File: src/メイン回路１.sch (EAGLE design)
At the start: 34 parts, among them T1 一般的なトランジスタ, T2 一般的なトランジスタ, T3 一般的なトランジスタ, T4 一般的なトランジスタ

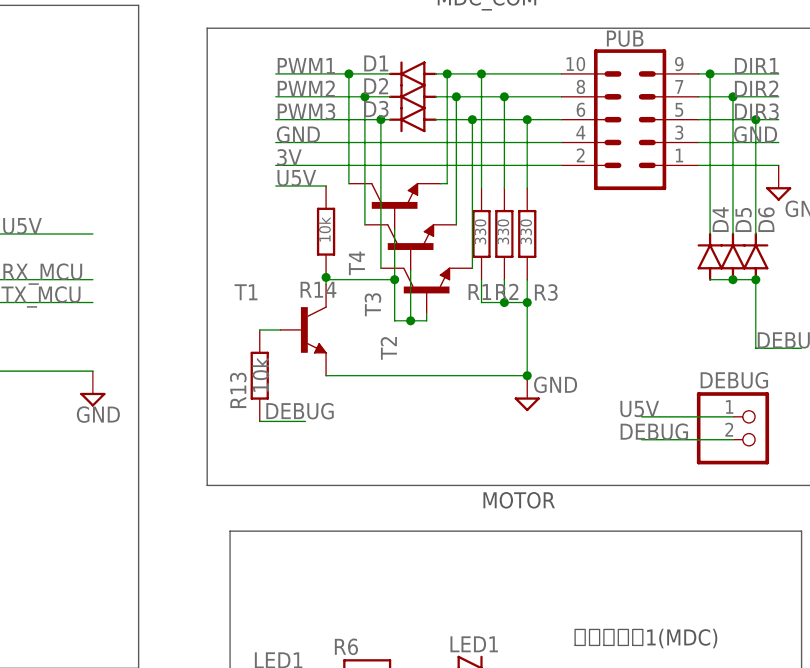
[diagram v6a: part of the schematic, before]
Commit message: 暴走対策機能付き非常停止スイッチの回路のガバを修復
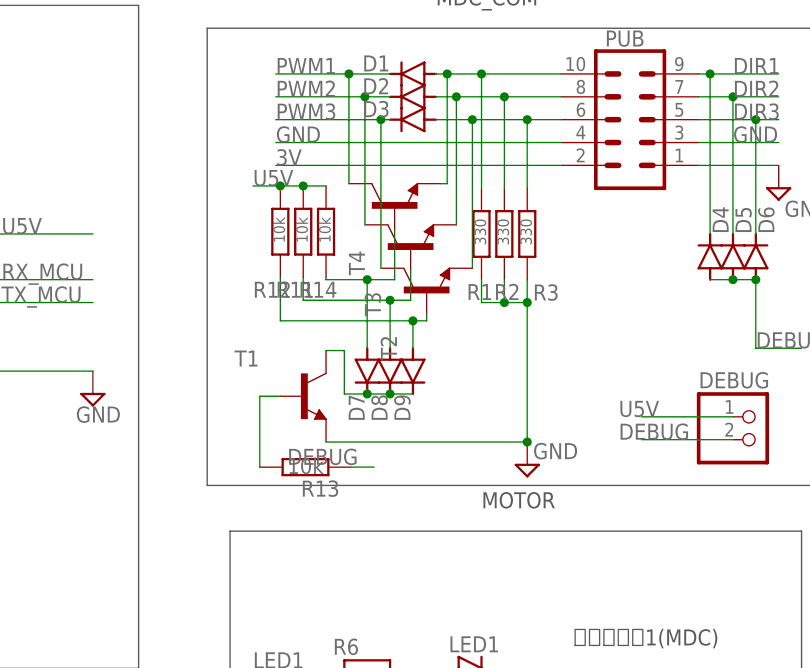
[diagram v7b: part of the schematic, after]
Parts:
- added D7, D8, D9: 1N4004, diode:1N4004
- added R11, R12: 10k, rcl:R-EU_0204/7
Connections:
- new net N$5: D8.A, R11.1, T3.B
- new net N$6: D9.A, R12.1, T2.B
- new net N$7: D7.C, D8.C, D9.C, T1.C
- net U5V: now also R11.2, R12.2
- net ZM: now also D7.A; no longer T1.C, T2.B, T3.B
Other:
- moved on the sheet: R13, T1
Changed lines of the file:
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@@
 <part name="T4" library="一般的なトランジスタ" deviceset="一般的なトランジスタ" device=""/>
 <part name="ソケット置き" library="pinhead" library_urn="urn:adsk.eagle:library:325" deviceset="PINHD-1X2" device="" package3d_urn="urn:adsk.eagle:package:22435/2"/>
+<part name="R11" library="rcl" library_urn="urn:adsk.eagle:library:334" deviceset="R-EU_" device="0204/7" package3d_urn="urn:adsk.eagle:package:23498/2" value="10k"/>
+<part name="R12" library="rcl" library_urn="urn:adsk.eagle:library:334" deviceset="R-EU_" device="0204/7" package3d_urn="urn:adsk.eagle:package:23498/2" value="10k"/>
+<part name="D7" library="diode" library_urn="urn:adsk.eagle:library:210" deviceset="1N4004" device="" package3d_urn="urn:adsk.eagle:package:43336/1"/>
+<part name="D8" library="diode" library_urn="urn:adsk.eagle:library:210" deviceset="1N4004" device="" package3d_urn="urn:adsk.eagle:package:43336/1"/>
+<part name="D9" library="diode" library_urn="urn:adsk.eagle:library:210" deviceset="1N4004" device="" package3d_urn="urn:adsk.eagle:package:43336/1"/>
 </parts>
 <sheets>
@@
 <attribute name="SHEET" x="230.505" y="5.08" size="2.54" layer="94"/>
 </instance>
-<instance part="SUPPLY1" gate="GND" x="215.9" y="85.852" smashed="yes">
-<attribute name="VALUE" x="216.535" y="86.487" size="1.778" layer="96"/>
+<instance part="SUPPLY1" gate="GND" x="215.9" y="78.486" smashed="yes">
+<attribute name="VALUE" x="216.535" y="79.121" size="1.778" layer="96"/>
 </instance>
 <instance part="MDC" gate="G$1" x="223.52" y="142.24" smashed="yes" rot="R180">
@@
 <attribute name="VALUE" x="234.95" y="76.2" size="1.778" layer="96"/>
 </instance>
-<instance part="R13" gate="G$1" x="186.182" y="88.392" smashed="yes" rot="R90">
-<attribute name="NAME" x="184.6834" y="84.582" size="1.778" layer="95" rot="R90"/>
-<attribute name="VALUE" x="187.198" y="86.36" size="1.778" layer="96" rot="R90"/>
+<instance part="R13" gate="G$1" x="191.262" y="78.232" smashed="yes" rot="R180">
+<attribute name="NAME" x="195.072" y="76.7334" size="1.778" layer="95" rot="R180"/>
+<attribute name="VALUE" x="193.294" y="79.248" size="1.778" layer="96" rot="R180"/>
 </instance>
 <instance part="D1" gate="1" x="203.2" y="121.92" smashed="yes" rot="R180">
@@
 <attribute name="NAME" x="243.3574" y="104.14" size="1.778" layer="95" rot="R90"/>
 </instance>
-<instance part="T1" gate="G$1" x="191.008" y="93.472" smashed="yes">
-<attribute name="NAME" x="183.388" y="96.774" size="1.778" layer="95"/>
+<instance part="T1" gate="G$1" x="191.008" y="86.106" smashed="yes">
+<attribute name="NAME" x="183.388" y="89.408" size="1.778" layer="95"/>
 </instance>
 <instance part="T2" gate="G$1" x="204.724" y="97.79" smashed="yes" rot="R90">
@@
 <attribute name="NAME" x="49.53" y="159.385" size="1.778" layer="95" rot="R180"/>
 <attribute name="VALUE" x="46.99" y="170.18" size="1.778" layer="96" rot="R180"/>
+</instance>
+<instance part="R11" gate="G$1" x="191.008" y="104.394" smashed="yes" rot="R90">
+<attribute name="NAME" x="192.278" y="98.8314" size="1.778" layer="95" rot="R180"/>
+<attribute name="VALUE" x="191.516" y="103.124" size="1.27" layer="96" rot="R90"/>
+</instance>
+<instance part="R12" gate="G$1" x="188.468" y="104.394" smashed="yes" rot="R90">
+<attribute name="NAME" x="189.738" y="98.8314" size="1.778" layer="95" rot="R180"/>
+<attribute name="VALUE" x="188.976" y="103.124" size="1.27" layer="96" rot="R90"/>
+</instance>
+<instance part="D7" gate="1" x="198.12" y="88.9" smashed="yes" rot="R270">
+<attribute name="NAME" x="196.0626" y="86.36" size="1.778" layer="95" rot="R270"/>
+</instance>
+<instance part="D8" gate="1" x="200.66" y="88.9" smashed="yes" rot="R270">
+<attribute name="NAME" x="198.6026" y="86.36" size="1.778" layer="95" rot="R270"/>
+</instance>
+<instance part="D9" gate="1" x="203.2" y="88.9" smashed="yes" rot="R270">
+<attribute name="NAME" x="201.1426" y="86.36" size="1.778" layer="95" rot="R270"/>
 </instance>
 </instances>
@@
 <segment>
 <pinref part="SUPPLY1" gate="GND" pin="GND"/>
-<wire x1="215.9" y1="88.392" x2="215.9" y2="96.52" width="0.1524" layer="91"/>
+<wire x1="215.9" y1="81.026" x2="215.9" y2="96.52" width="0.1524" layer="91"/>
 <wire x1="215.9" y1="96.52" x2="213.36" y2="96.52" width="0.1524" layer="91"/>
 <wire x1="213.36" y1="96.52" x2="210.82" y2="96.52" width="0.1524" layer="91"/>
@@
 <pinref part="R2" gate="G$1" pin="1"/>
 <pinref part="R3" gate="G$1" pin="1"/>
-<wire x1="193.548" y1="88.392" x2="215.9" y2="88.392" width="0.1524" layer="91"/>
-<junction x="215.9" y="88.392"/>
+<wire x1="193.548" y1="81.026" x2="215.9" y2="81.026" width="0.1524" layer="91"/>
+<junction x="215.9" y="81.026"/>
 <pinref part="T1" gate="G$1" pin="E"/>
 </segment>
@@
 <segment>
 <pinref part="R14" gate="G$1" pin="2"/>
-<wire x1="193.548" y1="109.474" x2="187.96" y2="109.474" width="0.1524" layer="91"/>
-<label x="187.96" y="109.474" size="1.778" layer="95"/>
+<wire x1="193.548" y1="109.474" x2="191.008" y2="109.474" width="0.1524" layer="91"/>
+<label x="185.42" y="109.474" size="1.778" layer="95"/>
+<pinref part="R11" gate="G$1" pin="2"/>
+<wire x1="191.008" y1="109.474" x2="188.468" y2="109.474" width="0.1524" layer="91"/>
+<junction x="191.008" y="109.474"/>
+<pinref part="R12" gate="G$1" pin="2"/>
+<wire x1="188.468" y1="109.474" x2="185.42" y2="109.474" width="0.1524" layer="91"/>
+<junction x="188.468" y="109.474"/>
 </segment>
 </net>
@@
 <segment>
 <pinref part="R13" gate="G$1" pin="1"/>
-<wire x1="186.182" y1="83.312" x2="191.262" y2="83.312" width="0.1524" layer="91"/>
-<label x="186.69" y="83.566" size="1.778" layer="95"/>
+<wire x1="196.342" y1="78.232" x2="198.882" y2="78.232" width="0.1524" layer="91"/>
+<label x="189.23" y="78.486" size="1.778" layer="95"/>
 </segment>
 <segment>
@@
 <net name="ZM" class="0">
 <segment>
-<wire x1="201.168" y1="99.06" x2="201.168" y2="94.488" width="0.1524" layer="91"/>
-<wire x1="201.168" y1="94.488" x2="202.946" y2="94.488" width="0.1524" layer="91"/>
-<pinref part="T1" gate="G$1" pin="C"/>
-<pinref part="R14" gate="G$1" pin="1"/>
-<wire x1="202.946" y1="94.488" x2="204.724" y2="94.488" width="0.1524" layer="91"/>
-<wire x1="193.548" y1="98.552" x2="193.548" y2="99.314" width="0.1524" layer="91"/>
-<wire x1="193.548" y1="99.314" x2="193.548" y2="99.06" width="0.1524" layer="91"/>
-<wire x1="193.548" y1="99.06" x2="201.168" y2="99.06" width="0.1524" layer="91"/>
-<junction x="193.548" y="99.314"/>
-<pinref part="T2" gate="G$1" pin="B"/>
-<wire x1="204.724" y1="95.25" x2="204.724" y2="94.488" width="0.1524" layer="91"/>
-<pinref part="T3" gate="G$1" pin="B"/>
-<wire x1="202.946" y1="100.076" x2="202.946" y2="94.488" width="0.1524" layer="91"/>
-<junction x="202.946" y="94.488"/>
 <pinref part="T4" gate="G$1" pin="B"/>
 <wire x1="201.168" y1="104.648" x2="201.168" y2="99.06" width="0.1524" layer="91"/>
-<junction x="201.168" y="99.06"/>
-</segment>
-</net>
-<net name="N$4" class="0">
-<segment>
-<pinref part="R13" gate="G$1" pin="2"/>
-<wire x1="188.468" y1="93.472" x2="186.182" y2="93.472" width="0.1524" layer="91"/>
-<pinref part="T1" gate="G$1" pin="B"/>
+<pinref part="R14" gate="G$1" pin="1"/>
+<wire x1="201.168" y1="99.06" x2="198.12" y2="99.06" width="0.1524" layer="91"/>
+<wire x1="198.12" y1="99.06" x2="193.548" y2="99.06" width="0.1524" layer="91"/>
+<wire x1="193.548" y1="99.06" x2="193.548" y2="99.314" width="0.1524" layer="91"/>
+<pinref part="D7" gate="1" pin="A"/>
+<wire x1="198.12" y1="91.44" x2="198.12" y2="99.06" width="0.1524" layer="91"/>
+<junction x="198.12" y="99.06"/>
 </segment>
 </net>
@@
 </segment>
 </net>
+<net name="N$6" class="0">
+<segment>
+<pinref part="T2" gate="G$1" pin="B"/>
+<wire x1="204.724" y1="95.25" x2="204.724" y2="94.488" width="0.1524" layer="91"/>
+<pinref part="R12" gate="G$1" pin="1"/>
+<wire x1="188.468" y1="99.314" x2="188.468" y2="94.488" width="0.1524" layer="91"/>
+<wire x1="188.468" y1="94.488" x2="203.2" y2="94.488" width="0.1524" layer="91"/>
+<pinref part="D9" gate="1" pin="A"/>
+<wire x1="203.2" y1="94.488" x2="204.724" y2="94.488" width="0.1524" layer="91"/>
+<wire x1="203.2" y1="91.44" x2="203.2" y2="94.488" width="0.1524" layer="91"/>
+<junction x="203.2" y="94.488"/>
+</segment>
+</net>
+<net name="N$5" class="0">
+<segment>
+<pinref part="R11" gate="G$1" pin="1"/>
+<wire x1="191.008" y1="99.314" x2="191.008" y2="96.774" width="0.1524" layer="91"/>
+<wire x1="191.008" y1="96.774" x2="200.66" y2="96.774" width="0.1524" layer="91"/>
+<wire x1="200.66" y1="96.774" x2="202.946" y2="96.774" width="0.1524" layer="91"/>
+<wire x1="202.946" y1="96.774" x2="202.946" y2="100.076" width="0.1524" layer="91"/>
+<pinref part="T3" gate="G$1" pin="B"/>
+<pinref part="D8" gate="1" pin="A"/>
+<wire x1="200.66" y1="91.44" x2="200.66" y2="96.774" width="0.1524" layer="91"/>
+<junction x="200.66" y="96.774"/>
+</segment>
+</net>
+<net name="N$4" class="0">
+<segment>
+<pinref part="T1" gate="G$1" pin="B"/>
+<pinref part="R13" gate="G$1" pin="2"/>
+<wire x1="188.468" y1="86.106" x2="186.182" y2="86.106" width="0.1524" layer="91"/>
+<wire x1="186.182" y1="86.106" x2="186.182" y2="78.232" width="0.1524" layer="91"/>
+</segment>
+</net>
+<net name="N$7" class="0">
+<segment>
+<pinref part="D7" gate="1" pin="C"/>
+<pinref part="D9" gate="1" pin="C"/>
+<wire x1="198.12" y1="86.36" x2="200.66" y2="86.36" width="0.1524" layer="91"/>
+<pinref part="D8" gate="1" pin="C"/>
+<wire x1="200.66" y1="86.36" x2="203.2" y2="86.36" width="0.1524" layer="91"/>
+<junction x="200.66" y="86.36"/>
+<wire x1="198.12" y1="86.36" x2="195.58" y2="86.36" width="0.1524" layer="91"/>
+<wire x1="195.58" y1="86.36" x2="195.58" y2="91.186" width="0.1524" layer="91"/>
+<junction x="198.12" y="86.36"/>
+<wire x1="195.58" y1="91.186" x2="193.548" y2="91.186" width="0.1524" layer="91"/>
+<pinref part="T1" gate="G$1" pin="C"/>
+</segment>
+</net>

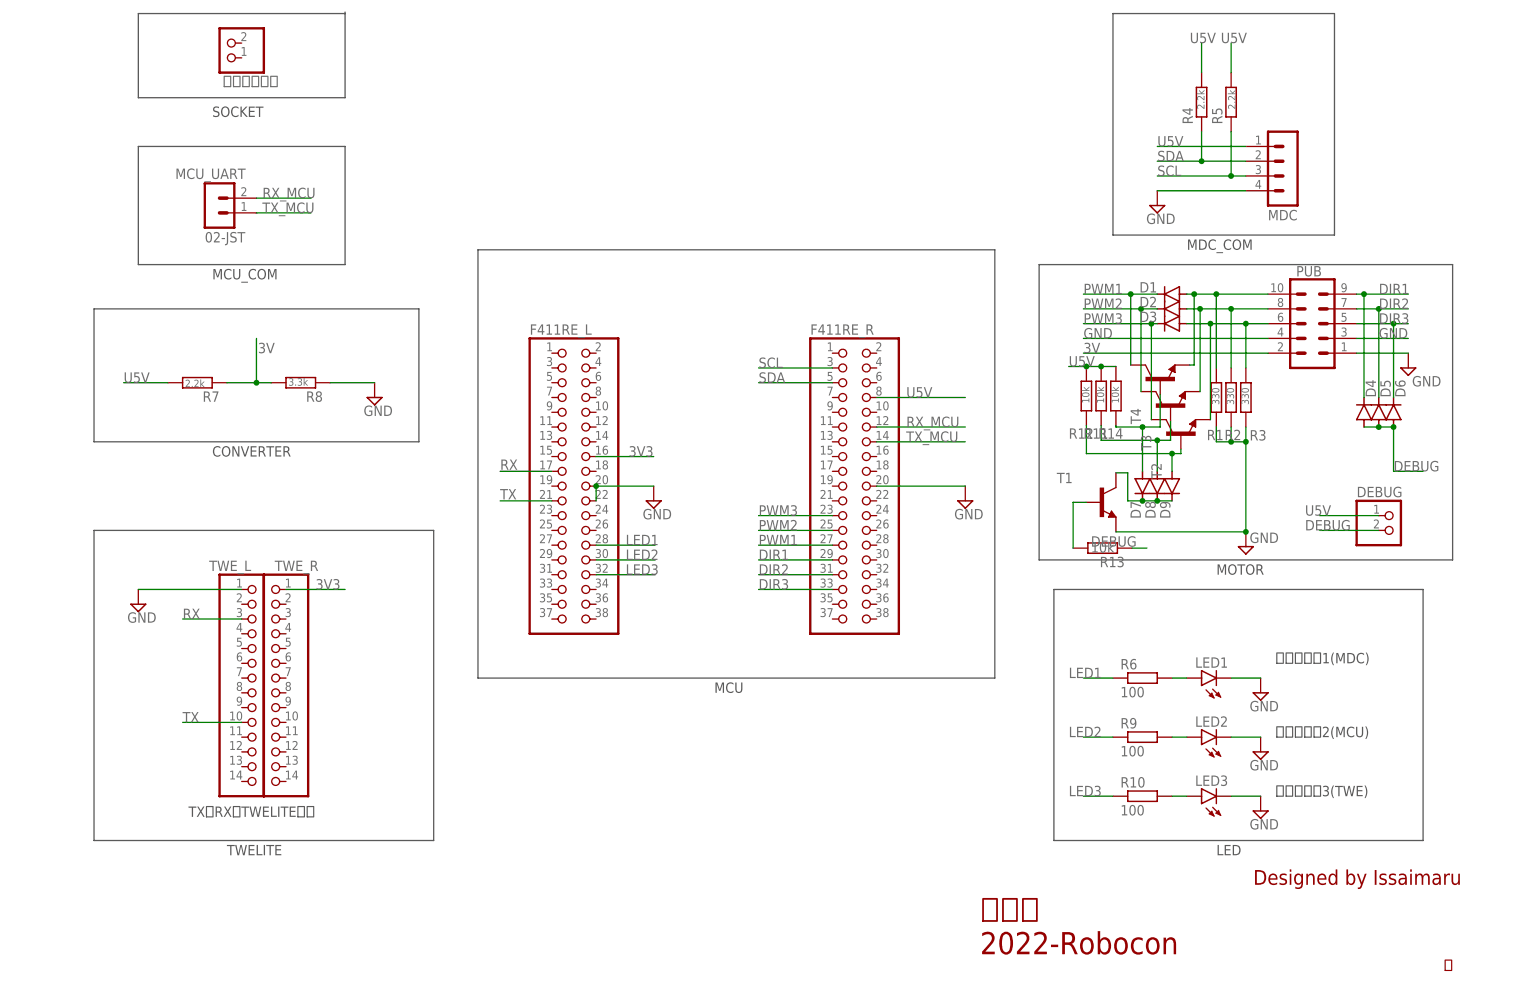
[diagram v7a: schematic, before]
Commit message: 配線をDriveUnit ver2.0用に変更
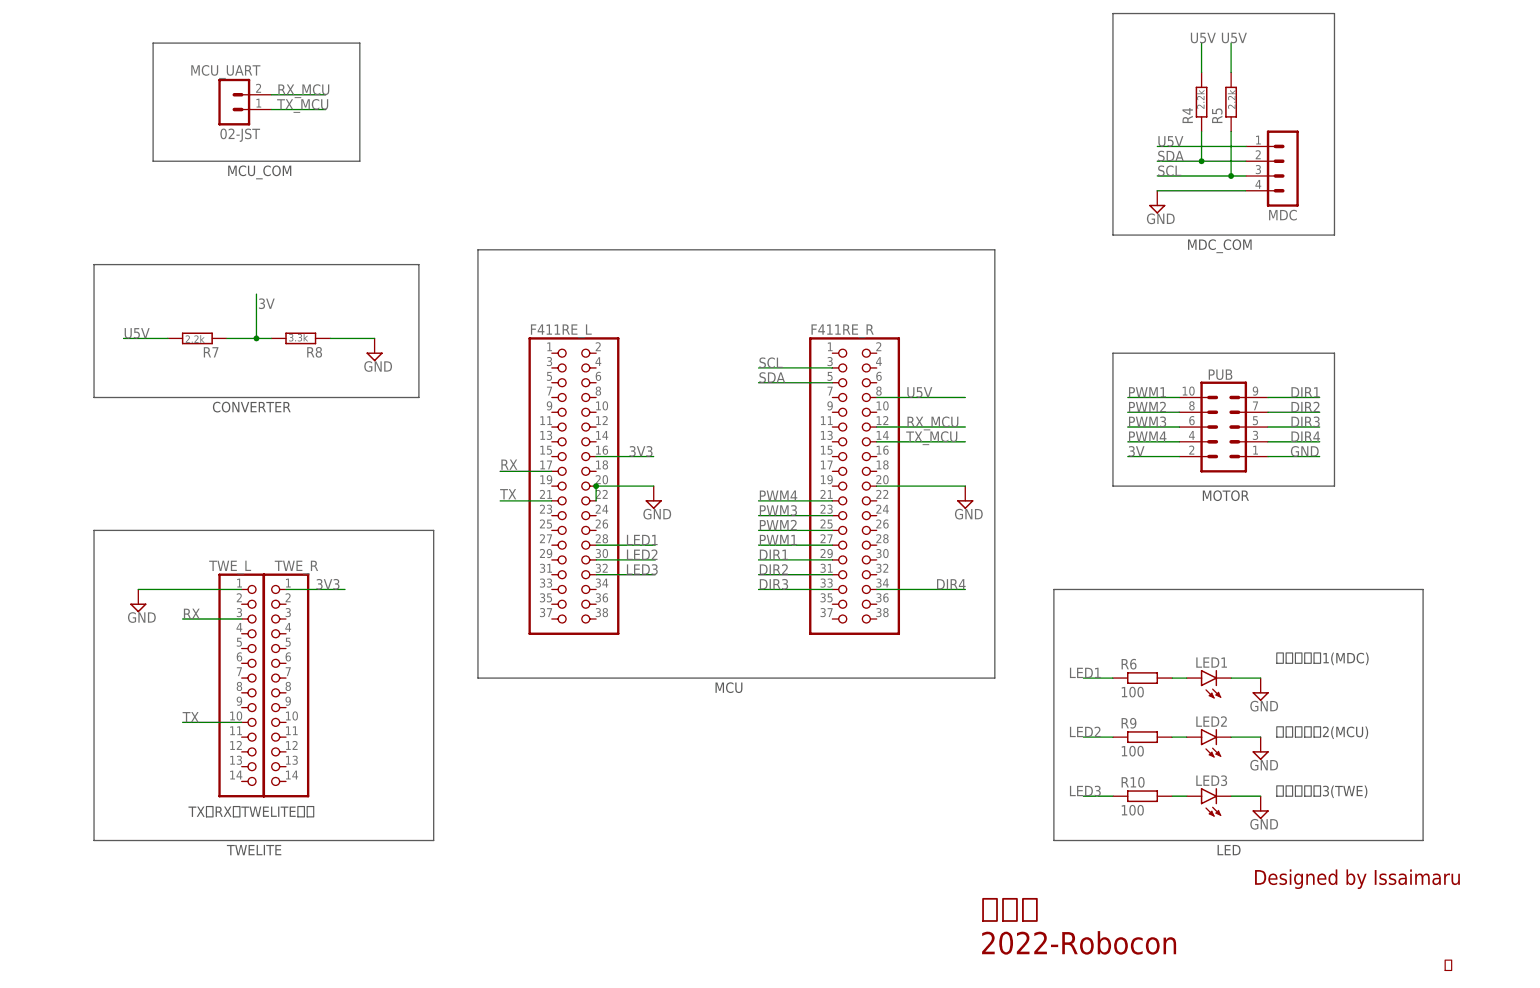
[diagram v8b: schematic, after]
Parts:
- removed D1, D2, D3, D4, D5, D6, D7, D8, D9: 1N4004, diode:1N4004
- removed DEBUG, ソケット置き: (no value), pinhead:PINHD-1X2
- removed R1, R2, R3: 330, rcl:R-EU_0204/7
- removed R11, R12, R13, R14: 10k, rcl:R-EU_0204/7
- removed T1, T2, T3, T4: 一般的なトランジスタ, 一般的なトランジスタ:一般的なトランジスタ
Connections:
- removed net DEBUG: D4.A, D5.A, D6.A, DEBUG.2, R13.1
- removed net N$4: R13.2, T1.B
- removed net N$5: D8.A, R11.1, T3.B
- removed net N$6: D9.A, R12.1, T2.B
- removed net N$7: D7.C, D8.C, D9.C, T1.C
- removed net N$8: D1.A, PUB.10, R1.2, T4.E
- removed net N$9: D2.A, PUB.8, R2.2, T3.E
- removed net N$Q0: D3.A, PUB.6, R3.2, T2.E
- removed net ZM: D7.A, R14.1, T4.B
- new net DIR4: F411RE_R.34, PUB.3
- new net PWM4: F411RE_R.21, PUB.4
- net DIR1: no longer D4.C
- net DIR2: no longer D5.C
- net DIR3: no longer D6.C
- net GND: no longer PUB.3, PUB.4, R1.1, R2.1, R3.1, T1.E
- net PWM1: now also PUB.10; no longer D1.C, T4.C
- net PWM2: now also PUB.8; no longer D2.C, T3.C
- net PWM3: now also PUB.6; no longer D3.C, T2.C
- net U5V: no longer DEBUG.1, R11.2, R12.2, R14.2
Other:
- note removed: "SOCKET"
- moved on the sheet: MCU_UART, PUB, R7, R8
